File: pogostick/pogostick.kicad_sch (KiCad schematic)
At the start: 0 parts

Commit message: Add .gitignore file
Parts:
- added H1: MountingHole_Pad, MountingHole:MountingHole_3.2mm_M3_ISO7380_Pad_TopBottom, symbol Mechanical:MountingHole_Pad

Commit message: First iteration of board
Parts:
- added H2: M3_MountingHole_Pad, MountingHole:MountingHole_3.2mm_M3_ISO7380_Pad_TopBottom, symbol Mechanical:MountingHole_Pad
- added H3, H4, H5: MountingHole, MountingHole:MountingHole_3.2mm_M3, symbol Mechanical:MountingHole
- added J1, J10, J11, J12, J13, J14, J15, J16, J17, J18, J19, J2, J20, J21, J22, J23, J24, J25, J26, J27, J28, J29, J3, J30, J31, J32, J33, J34, J35, J36, J37, J38, J39, J4, J40, J41, J42, J43, J44, J45, J46, J47, J48, J49, J5, J50, J51, J52, J53, J54, J55, J56, J57, J58, J59, J6, J60, J7, J8, J9: Pogo pin, pogostick:PogoPin_Pad_D1.83mm, symbol Connector:Conn_01x01_Pin
- H1: value MountingHole_Pad -> M3_MountingHole_Pad
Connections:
- net pogo: now reaches H1.1
- net pogo: now also H2.1, J1.1 (Pin_1), J10.1 (Pin_1), J11.1 (Pin_1), J12.1 (Pin_1), J13.1 (Pin_1), J14.1 (Pin_1), J15.1 (Pin_1), J16.1 (Pin_1), J17.1 (Pin_1), J18.1 (Pin_1), J19.1 (Pin_1), J2.1 (Pin_1), J20.1 (Pin_1), J21.1 (Pin_1), J22.1 (Pin_1), J23.1 (Pin_1), J24.1 (Pin_1), J25.1 (Pin_1), J26.1 (Pin_1), J27.1 (Pin_1), J28.1 (Pin_1), J29.1 (Pin_1), J3.1 (Pin_1), J30.1 (Pin_1), J31.1 (Pin_1), J32.1 (Pin_1), J33.1 (Pin_1), J34.1 (Pin_1), J35.1 (Pin_1), J36.1 (Pin_1), J37.1 (Pin_1), J38.1 (Pin_1), J39.1 (Pin_1), J4.1 (Pin_1), J40.1 (Pin_1), J41.1 (Pin_1), J42.1 (Pin_1), J43.1 (Pin_1), J44.1 (Pin_1), J45.1 (Pin_1), J46.1 (Pin_1), J47.1 (Pin_1), J48.1 (Pin_1), J49.1 (Pin_1), J5.1 (Pin_1), J50.1 (Pin_1), J51.1 (Pin_1), J52.1 (Pin_1), J53.1 (Pin_1), J54.1 (Pin_1), J55.1 (Pin_1), J56.1 (Pin_1), J57.1 (Pin_1), J58.1 (Pin_1), J59.1 (Pin_1), J6.1 (Pin_1), J60.1 (Pin_1), J7.1 (Pin_1), J8.1 (Pin_1), J9.1 (Pin_1)
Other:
- moved on the sheet: H1

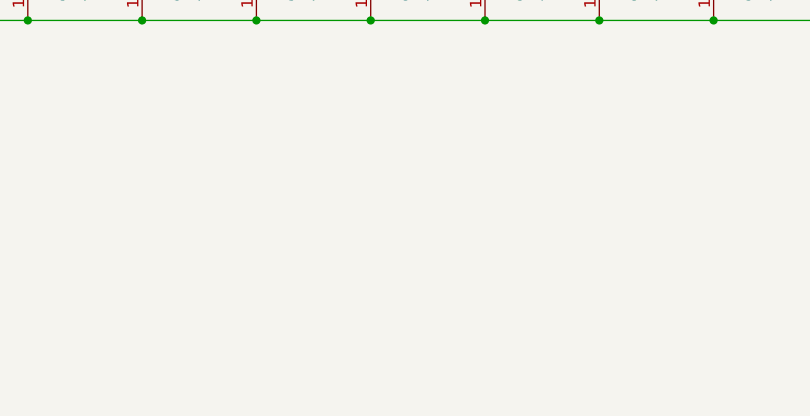
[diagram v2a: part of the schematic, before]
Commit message: Add top pour for thermals and regenerate gerbers
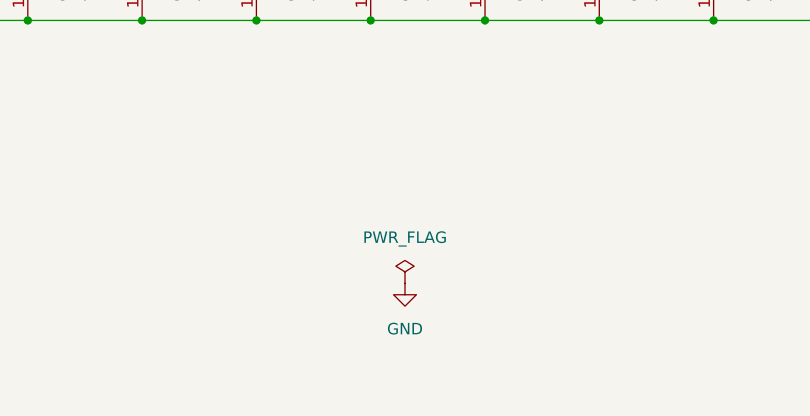
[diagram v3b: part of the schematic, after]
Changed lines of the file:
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@@
+	)
+	(symbol
+		(lib_id "power:GND")
+		(at 163.83 177.8 0)
+		(unit 1)
+		(body_style 1)
+		(exclude_from_sim no)
+		(in_bom yes)
+		(on_board yes)
+		(in_pos_files yes)
+		(dnp no)
+		(fields_autoplaced yes)
+		(property "Reference" "#PWR01"
+			(at 163.83 184.15 0)
+			(hide yes)
+			(show_name no)
+			(do_not_autoplace no)
+			(effects
+				(font
+					(size 1.27 1.27)
+				)
+			)
+		)
+		(property "Value" "GND"
+			(at 163.83 182.88 0)
+			(show_name no)
+			(do_not_autoplace no)
+			(effects
+				(font
+					(size 1.27 1.27)
+				)
+			)
+		)
+		(property "Footprint" ""
+			(at 163.83 177.8 0)
+			(hide yes)
+			(show_name no)
+			(do_not_autoplace no)
+			(effects
+				(font
+					(size 1.27 1.27)
+				)
+			)
+		)
+		(property "Datasheet" ""
+			(at 163.83 177.8 0)
+			(hide yes)
+			(show_name no)
+			(do_not_autoplace no)
+			(effects
+				(font
+					(size 1.27 1.27)
+				)
+			)
+		)
+		(property "Description" "Power symbol creates a global label with name \"GND\" , ground"
+			(at 163.83 177.8 0)
+			(hide yes)
+			(show_name no)
+			(do_not_autoplace no)
+			(effects
+				(font
+					(size 1.27 1.27)
+				)
+			)
+		)
+		(pin "1"
+		)
+		(instances
+			(project "pogostick"
+				(path "/da49594c-3040-4f48-9dcb-0efc03ccda83"
+					(reference "#PWR01")
+					(unit 1)
+				)
+			)
+		)
 	)
 	(symbol
@@
 					(unit 1)
 				)
+			)
+		)
+	)
+	(symbol
+		(lib_id "power:PWR_FLAG")
+		(at 163.83 177.8 0)
+		(unit 1)
+		(body_style 1)
+		(exclude_from_sim no)
+		(in_bom yes)
+		(on_board yes)
+		(in_pos_files yes)
+		(dnp no)
+		(fields_autoplaced yes)
+		(property "Reference" "#FLG01"
+			(at 163.83 175.895 0)
+			(hide yes)
+			(show_name no)
+			(do_not_autoplace no)
+			(effects
+				(font
+					(size 1.27 1.27)
+				)
+			)
+		)
+		(property "Value" "PWR_FLAG"
+			(at 163.83 172.72 0)
+			(show_name no)
+			(do_not_autoplace no)
+			(effects
+				(font
+					(size 1.27 1.27)
+				)
+			)
+		)
+		(property "Footprint" ""
+			(at 163.83 177.8 0)
+			(hide yes)
+			(show_name no)
+			(do_not_autoplace no)
+			(effects
+				(font
+					(size 1.27 1.27)
+				)
+			)
+		)
+		(property "Datasheet" ""
+			(at 163.83 177.8 0)
+			(hide yes)
+			(show_name no)
+			(do_not_autoplace no)
+			(effects
+				(font
+					(size 1.27 1.27)
+				)
+			)
+		)
+		(property "Description" "Special symbol for telling ERC where power comes from"
+			(at 163.83 177.8 0)
+			(hide yes)
+			(show_name no)
+			(do_not_autoplace no)
+			(effects
+				(font
+					(size 1.27 1.27)
+				)
+			)
+		)
+		(pin "1"
+		)
+		(instances
+			(project "pogostick"
+				(path "/da49594c-3040-4f48-9dcb-0efc03ccda83"
+					(reference "#FLG01")
+					(unit 1)
+				)

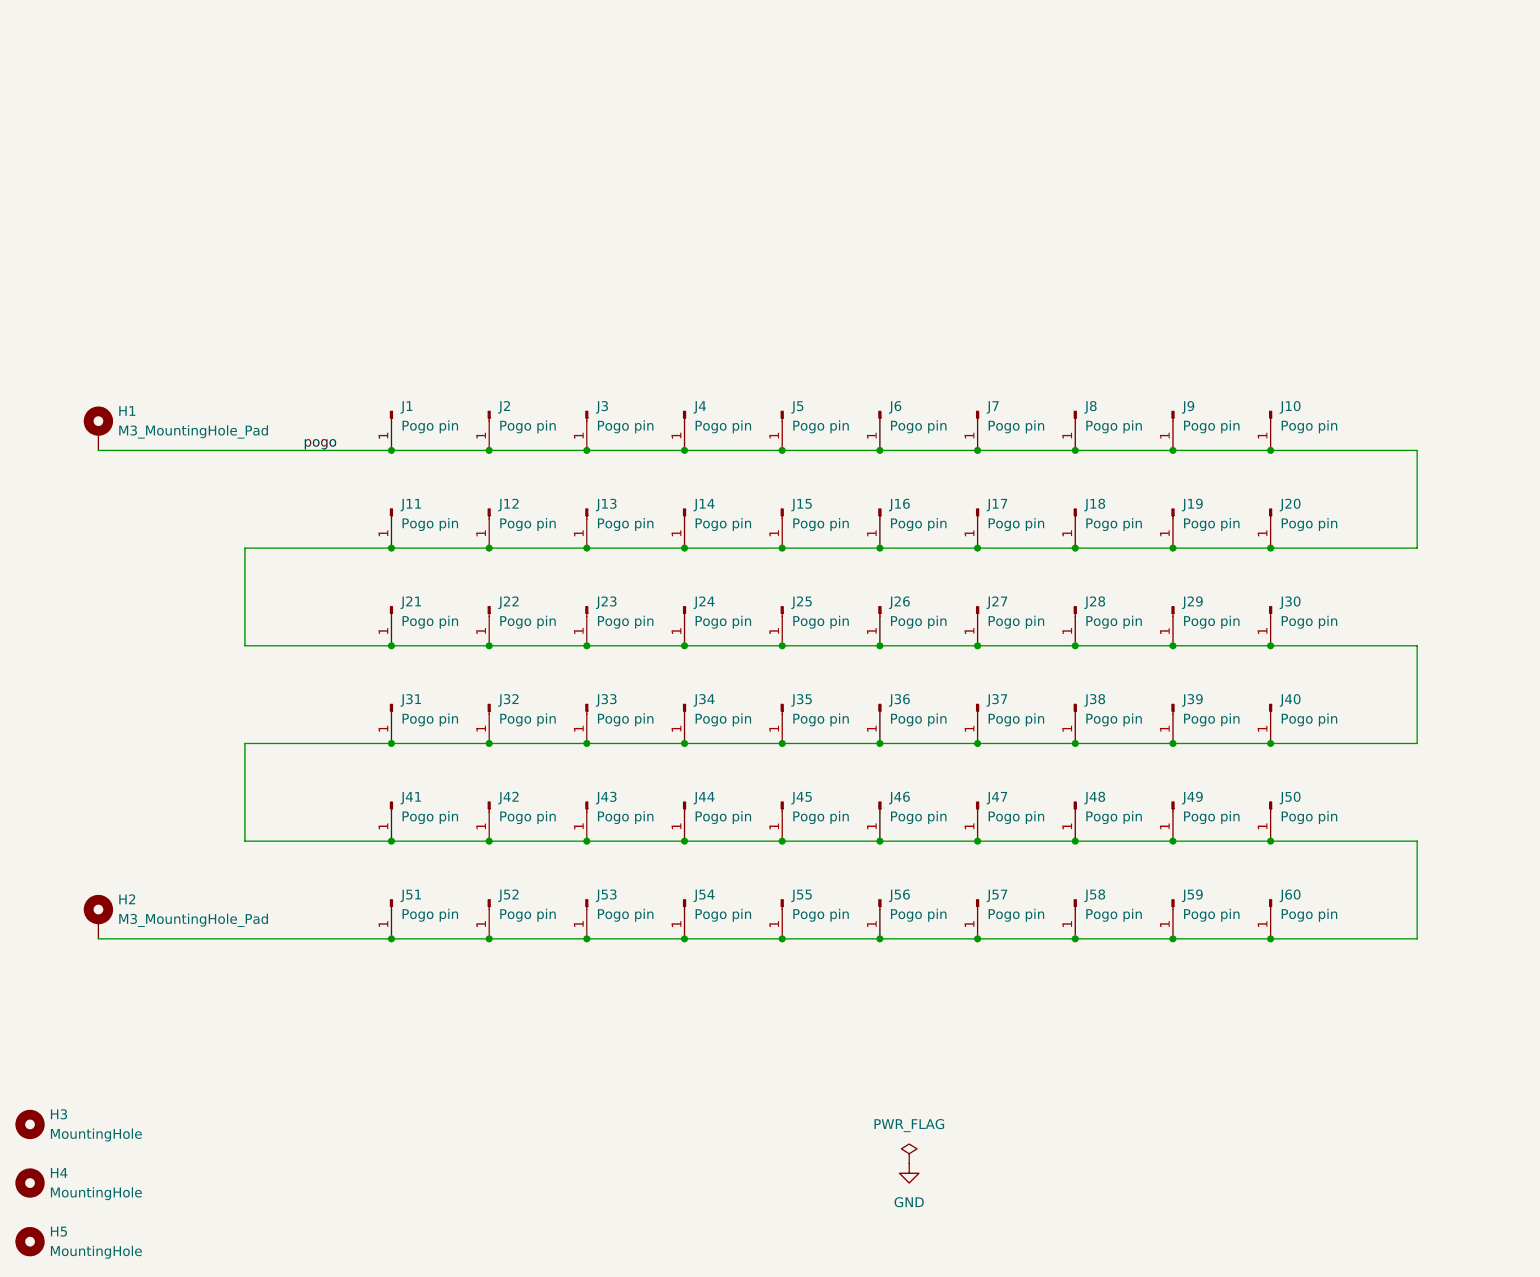
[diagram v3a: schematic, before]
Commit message: Add more images of board
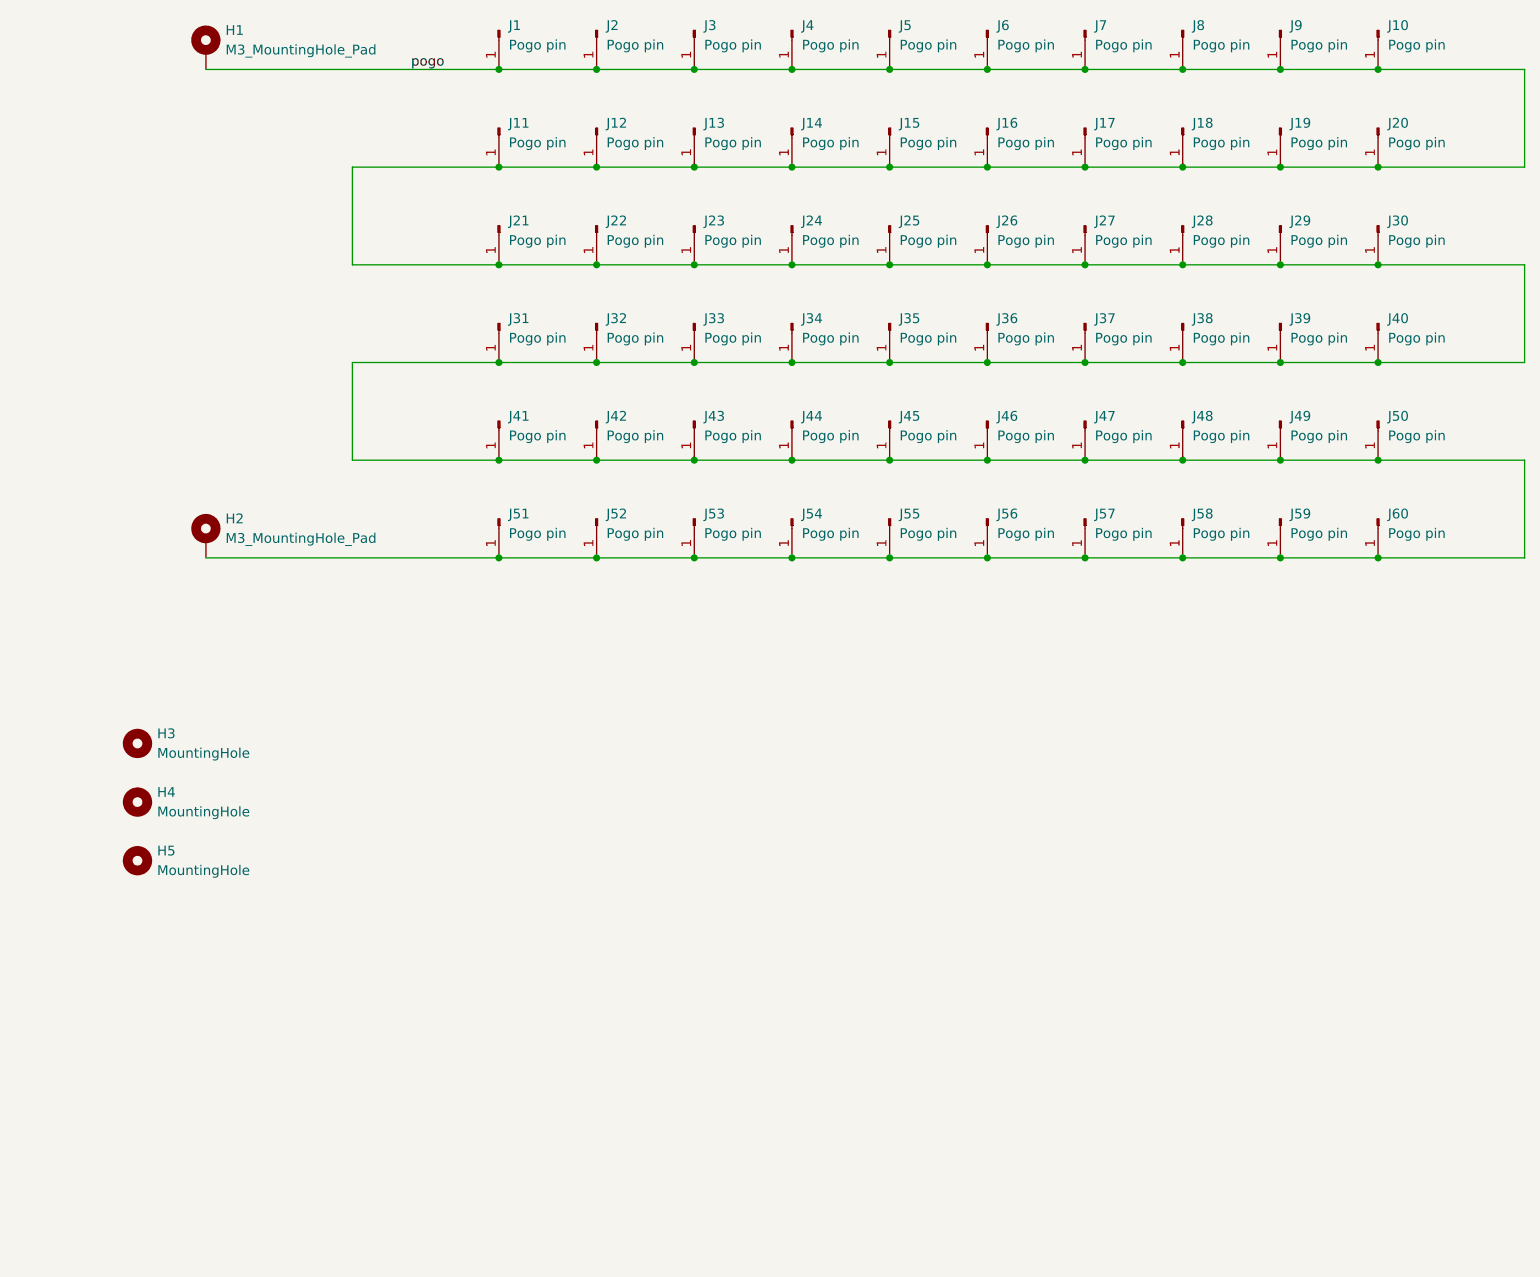
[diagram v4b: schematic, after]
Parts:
- H3, H4, H5: footprint MountingHole:MountingHole_3.2mm_M3 -> MountingHole:MountingHole_3.2mm_M3_ISO7380_Pad_TopBottom
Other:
- moved on the sheet: H1, H2, H3, H4, H5, J1, J10, J11, J12, J13, J14, J15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
